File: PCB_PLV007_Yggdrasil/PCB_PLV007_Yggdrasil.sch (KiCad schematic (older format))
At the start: 44 parts, among them J1 Conn_01x12, U1 BME280, U2 SN65HVD232

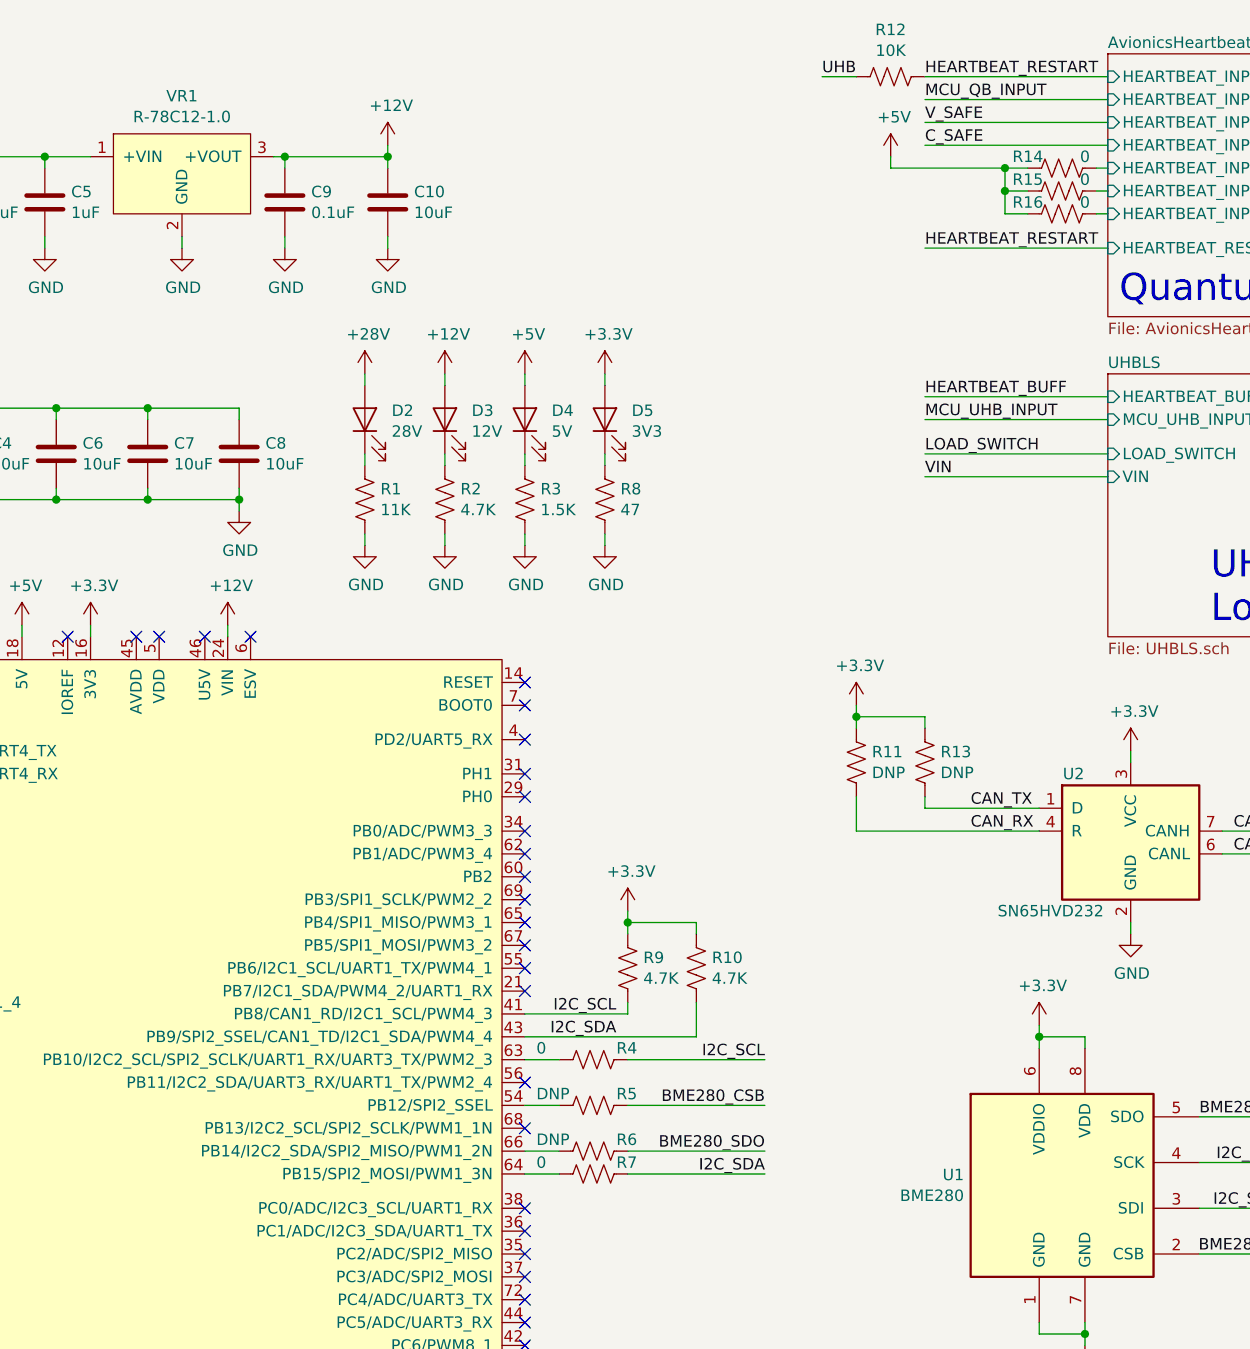
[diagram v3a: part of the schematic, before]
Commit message: Make Odin pass DRC, finish Yggdrasil
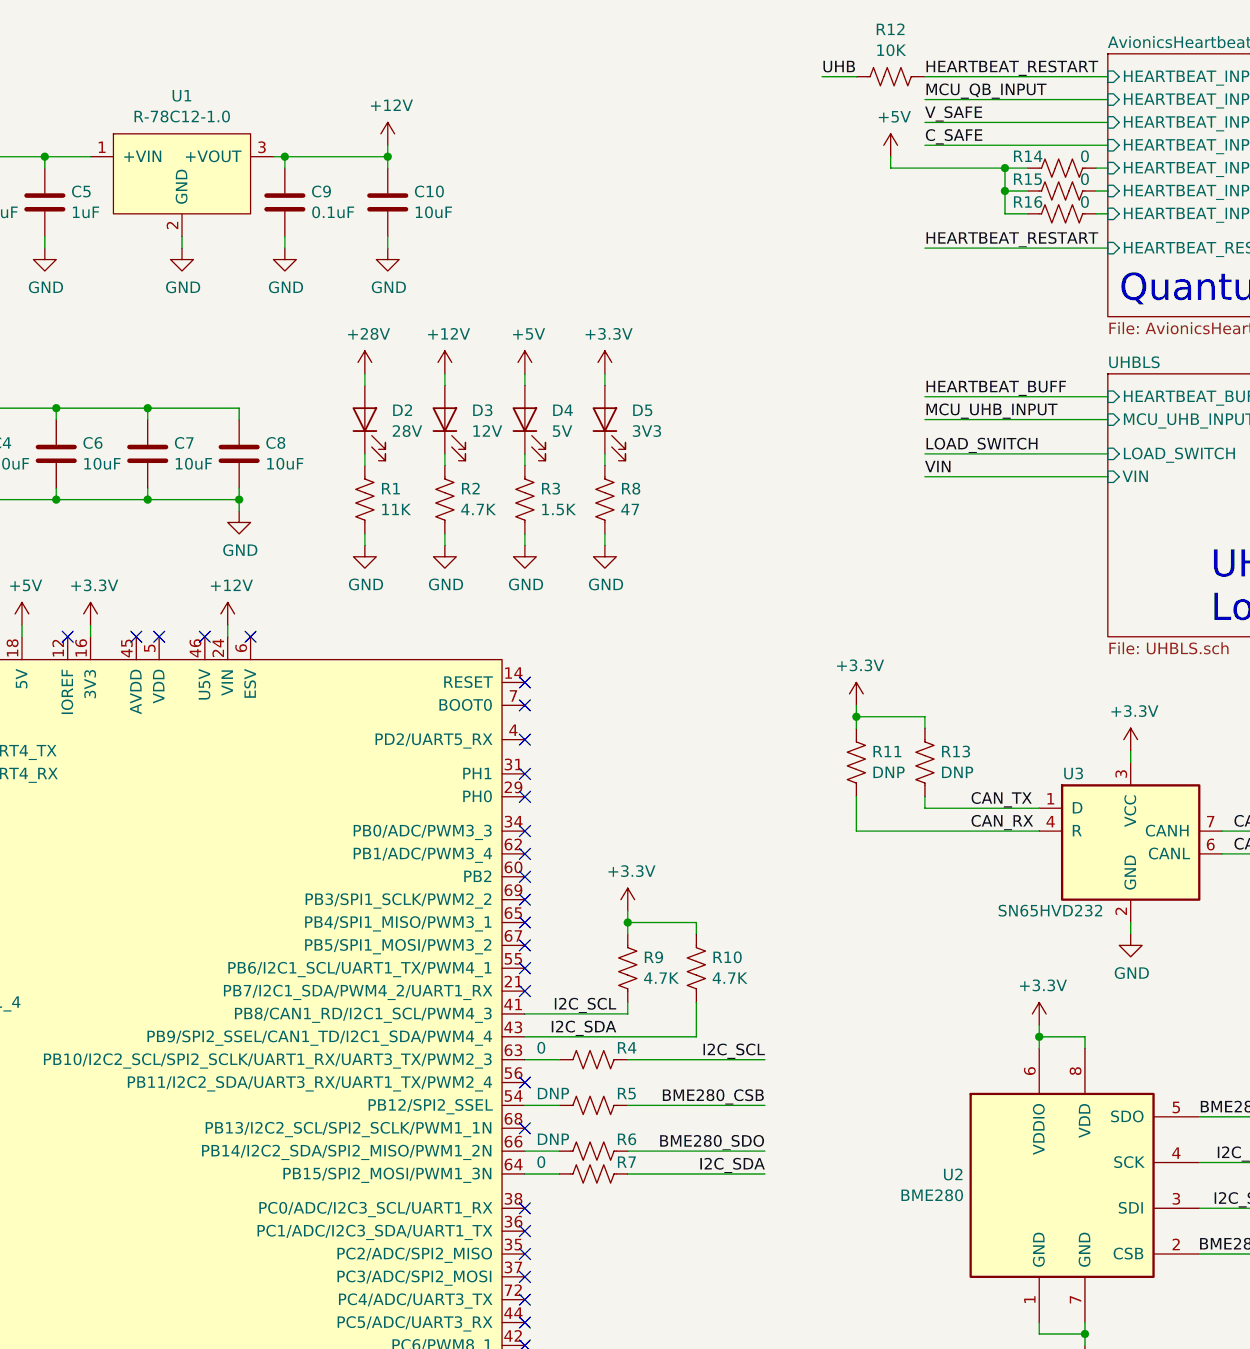
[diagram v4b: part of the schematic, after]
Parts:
- U1: renamed from VR1; footprint BoringFootprints:Recom_R-78c-1.0 -> BoringFootprints:Recom_R-78C-1.0
- renumbered U1 to U2, U2 to U3
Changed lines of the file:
@@
 Comp ""
 Comment1 "JKR"
-Comment2 "PLV007"
+Comment2 "PLV007_Yggdrasil"
 Comment3 ""
 Comment4 ""
@@
 QuantumBeat Slave
 $Comp
-L Interface_CAN_LIN:SN65HVD232 U2
+L Interface_CAN_LIN:SN65HVD232 U3
 U 1 1 5FB5123E
 P 7700 4100
-F 0 "U2" H 7450 4350 50  0000 C CNN
+F 0 "U3" H 7450 4350 50  0000 C CNN
 F 1 "SN65HVD232" H 7350 3750 50  0000 C CNN
 F 2 "Package_SO:SOIC-8_3.9x4.9mm_P1.27mm" H 7700 3600 50  0001 C CNN
@@
 	6000 7250 5050 7250
 $Comp
-L Sensor:BME280 U1
+L Sensor:BME280 U2
 U 1 1 5FC2E258
 P 7400 5650
-F 0 "U1" H 6971 5696 50  0000 R CNN
+F 0 "U2" H 6971 5696 50  0000 R CNN
 F 1 "BME280" H 6971 5605 50  0000 R CNN
 F 2 "Package_LGA:Bosch_LGA-8_2.5x2.5mm_P0.65mm_ClockwisePinNumbering" H 7400 5450 50  0001 C CNN
@@
 	9950 5900 9950 5950
 $Comp
-L boringlib:R-78C12-1.0 VR1
+L boringlib:R-78C12-1.0 U1
 U 1 1 5FD31019
 P 3550 1150
-F 0 "VR1" H 3550 1415 50  0000 C CNN
+F 0 "U1" H 3550 1415 50  0000 C CNN
 F 1 "R-78C12-1.0" H 3550 1324 50  0000 C CNN
-F 2 "BoringFootprints:Recom_R-78c-1.0" H 3750 850 50  0001 C CNN
+F 2 "BoringFootprints:Recom_R-78C-1.0" H 3750 850 50  0001 C CNN
 F 3 "https://recom-power.com/pdf/Innoline/R-78C-1.0.pdf" H 3750 850 50  0001 C CNN
 F 4 "R-78C12-1.0" H 3550 1150 50  0001 C CNN "MFPN"
